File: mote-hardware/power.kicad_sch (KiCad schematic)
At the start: 6 parts, among them J1 USB_C_Receptacle_USB2.0_14P, U2 NCP1117-3.3_SOT223

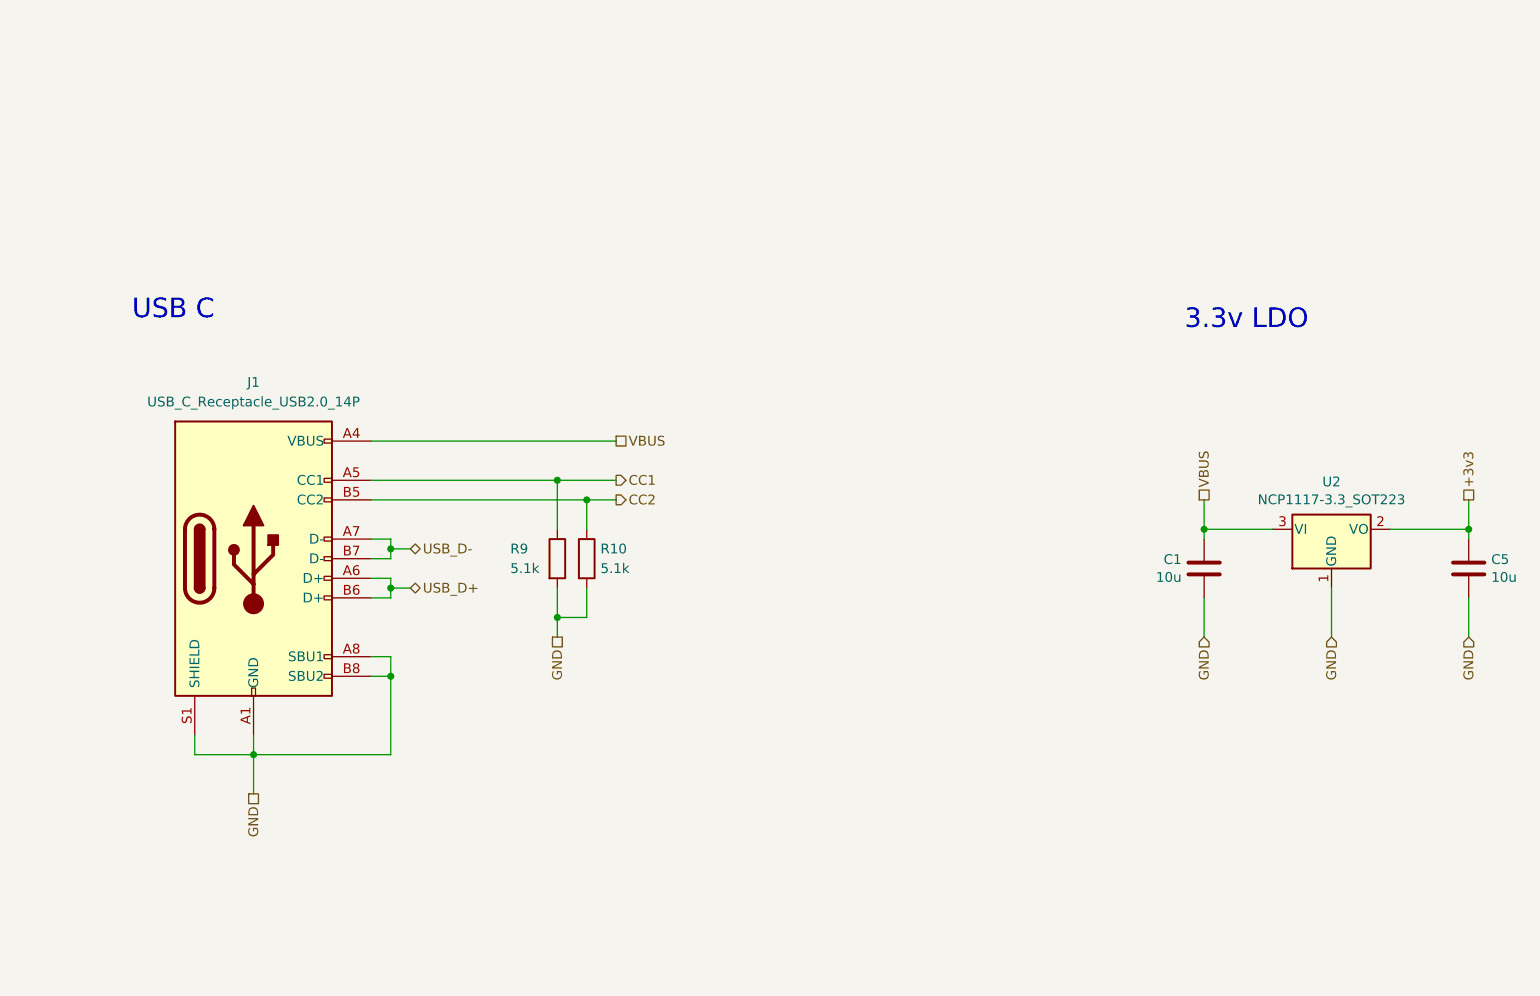
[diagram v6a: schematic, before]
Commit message: Hardware v0.1.0 updates (#52)
Addresses errata / improvements identified in
https://github.com/empriselab/mote-core/issues/37

---------

Co-authored-by: Kyle Mui <44453997+KyleMui@users.noreply.github.com>
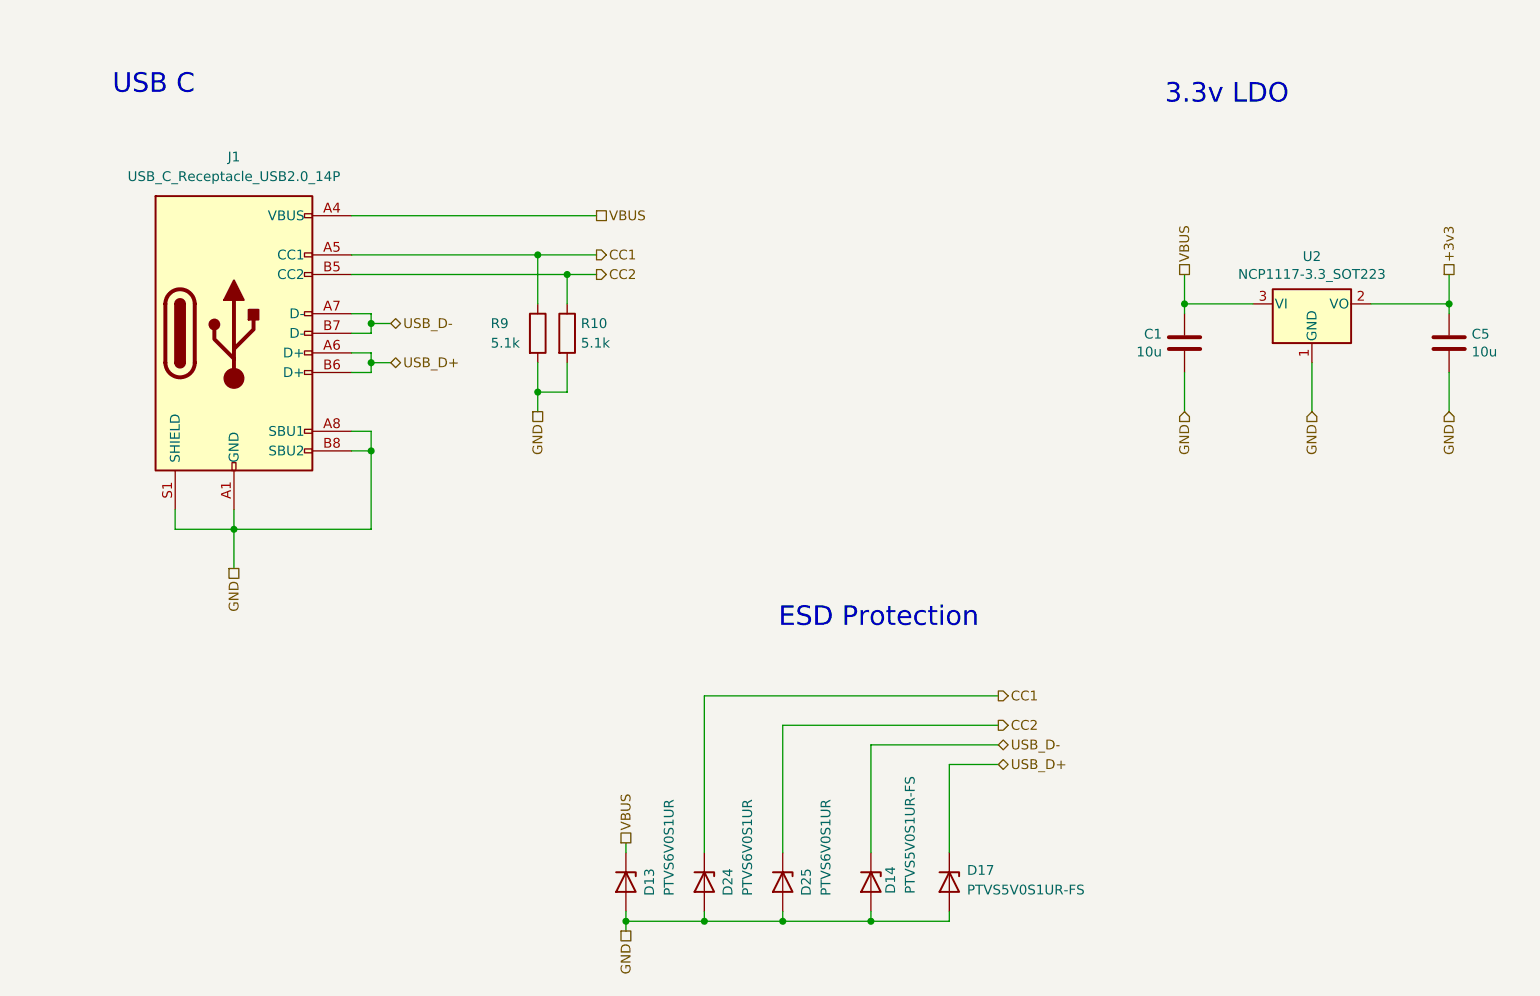
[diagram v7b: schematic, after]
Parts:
- added D13, D24, D25: PTVS6V0S1UR, Diode_SMD:D_SOD-123, symbol Diode:PTVS7V5Z1USK
- added D14, D17: PTVS5V0S1UR-FS, Diode_SMD:D_SOD-123, symbol Diode:PTVS5V0Z1USK
- C1, C5, R10, R9: JLCPCB_CORRECTION (none) -> 0; 0; 0
- J1: JLCPCB_CORRECTION (none) -> 0; -1.4605; 0
- U2: JLCPCB_CORRECTION (none) -> 0; 0; 180
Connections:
- net CC1: now also D24.1 (K)
- net CC2: now also D25.1 (K)
- net GND: now also D13.2 (A), D14.2 (A), D17.2 (A), D24.2 (A), D25.2 (A)
- net USB_D+: now also D17.1 (K)
- net USB_D-: now also D14.1 (K)
- net VBUS: now also D13.1 (K)
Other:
- note added: "ESD Protection"
- moved on the sheet: C1, C5, J1, R10, R9, U2
